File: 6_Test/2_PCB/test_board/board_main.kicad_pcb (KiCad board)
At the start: 4 copper layers, 93 parts, among them J1 PWR_Supply_Pins, J10 Chip_AVSS_GND_Jumpers, J11 Buffer_PWR_Jumper, J12 Reset_PWR_Jumpers, J13 Reset_Signal_Jumpers, J2 Analog_Input_Pins, J3 Digital_Input_Pins, J4 Digital_Output_Pins, J5 Chip_VDD_Jumpers, J6 BNC_Odd, J7 BNC_Even, J8 BNC_Jumpers, J9 Analog_Input_Jumpers, U1 TPS74501PDRVR, U2 ADA4807-1AKSZ-R7, U3 ADA4807-1AKSZ-R7, U4 TPS74501PDRVR, U5 SN74HC74DR, U6 CD4001BM96, U7 SN74ALVCH162827DLR

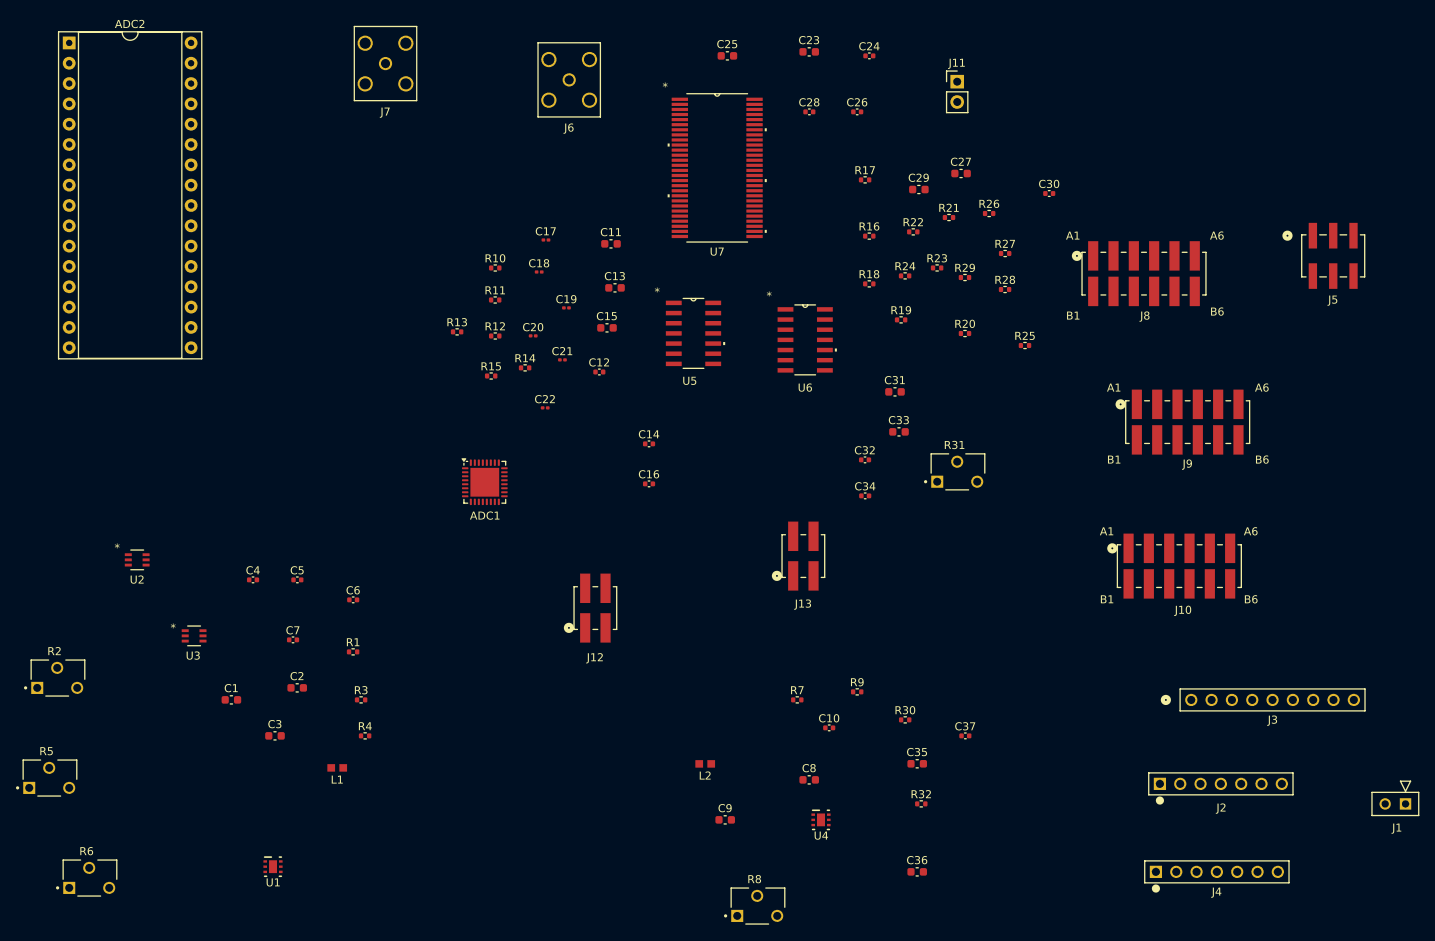
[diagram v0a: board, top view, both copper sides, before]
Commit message: Edit Layout 1_27
Rearranged the components in the layout and added majority of traces and ground layer. AVSS connections still need to be connected along with IOVDD
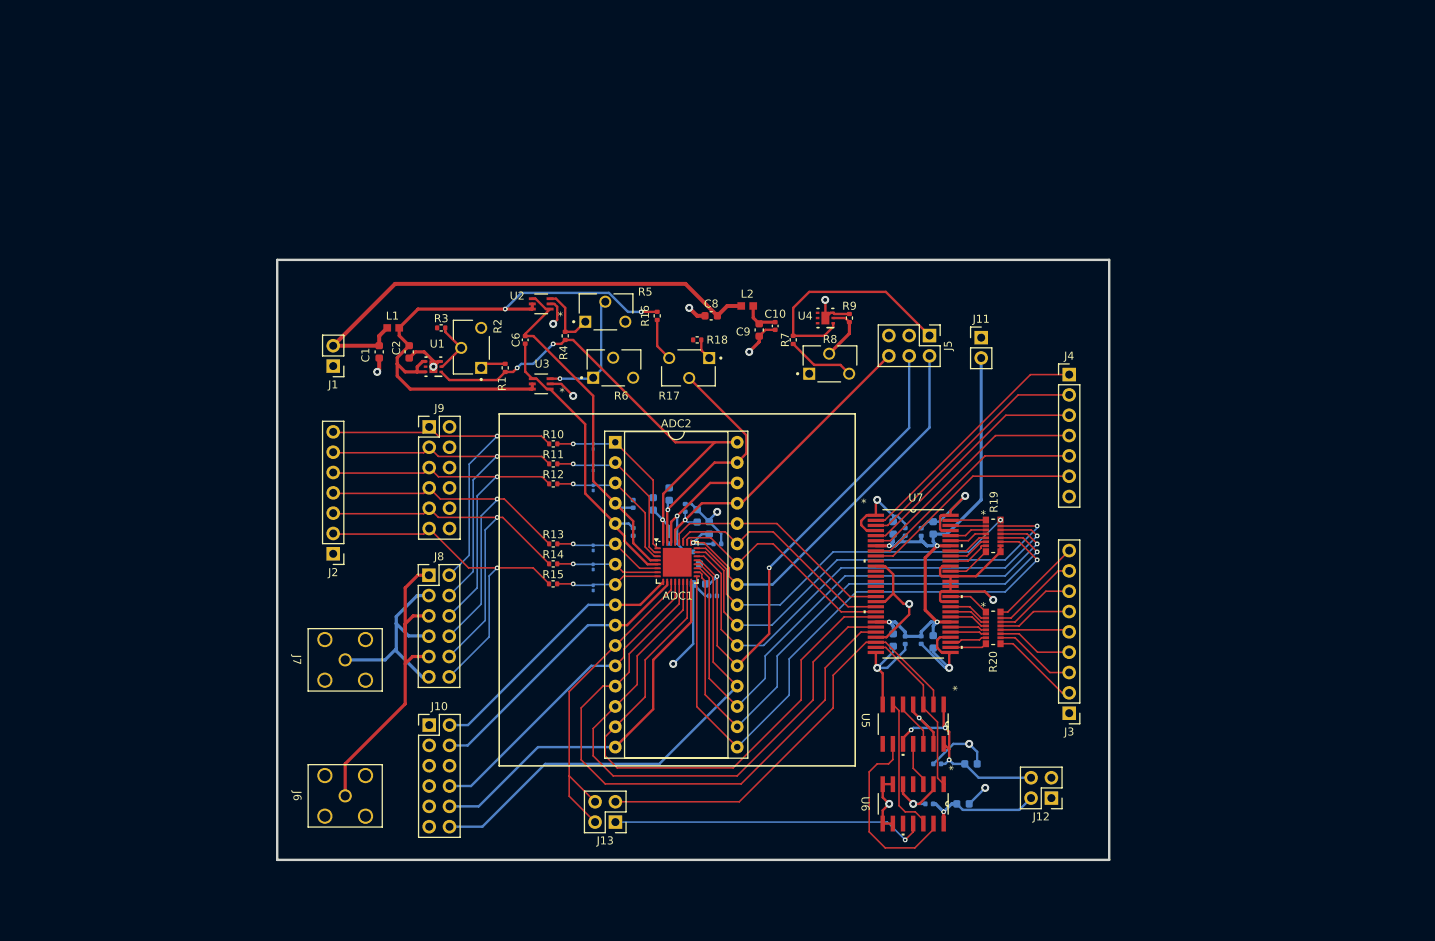
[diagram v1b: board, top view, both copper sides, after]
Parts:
- removed the R16 at (146.0, 61.5)
- removed the R17 at (145.5, 54.5)
- removed the R18 at (146.0, 67.5)
- removed R21, R22, R23, R24, R25, R26, R27, R28, R29: 22, Resistor_SMD:R_0402_1005Metric
- C11, C12, C13, C14, C15, C16, C17, C18, C19, C20, C21, C22, C23, C24, C25, C26, C27, C28, C29, C3, C30, C31, C32, C33, C34, C35, C36, C37, C4, C5, C7: moved to B.Cu
- J1: footprint ECE628_lib:1x2Header -> Connector_PinHeader_2.54mm:PinHeader_1x02_P2.54mm_Vertical
- J10, J8, J9: footprint ECE628_lib:2x6Header -> Connector_PinHeader_2.54mm:PinHeader_2x06_P2.54mm_Vertical
- J12, J13: footprint ECE628_lib:2x2Header -> Connector_PinHeader_2.54mm:PinHeader_2x02_P2.54mm_Vertical
- J2, J4: footprint ECE628_lib:1x7Header -> Connector_PinHeader_2.54mm:PinHeader_1x07_P2.54mm_Vertical
- J3: footprint ECE628_lib:1x9Header -> Connector_PinHeader_2.54mm:PinHeader_1x09_P2.54mm_Vertical
- J5: footprint ECE628_lib:2x3Header -> Connector_PinHeader_2.54mm:PinHeader_2x03_P2.54mm_Vertical
- R19, R20: value 22 -> EXB-2HV220JV; footprint Resistor_SMD:R_0402_1005Metric -> 22res_arrayFootprints:RES_EXB2HV
- moved J1 144.8 mm to (79.0, 77.8), turned to 180 degrees
- moved J2 107.3 mm to (79.0, 101.2), turned to 180 degrees
- moved J8 97.0 mm to (91.0, 103.9)
- moved J10 95.9 mm to (91.0, 122.7)
- moved J9 94.8 mm to (91.0, 85.4)
- moved J6 93.8 mm to (80.5, 131.5), turned to -90 degrees
- moved R6 91.4 mm to (114.0, 78.0)
- moved R5 90.7 mm to (113.0, 71.0)
- moved ADC2 84.6 mm to (114.3, 87.3)
- moved J7 74.7 mm to (80.5, 114.5), turned to -90 degrees
- moved R8 68.4 mm to (141.0, 77.5)
- moved C28 67.5 mm to (152.5, 112.0), turned to -90 degrees
- moved R2 66.2 mm to (96.3, 75.5), turned to 90 degrees
- moved U1 65.6 mm to (91.5, 77.8), turned to 180 degrees
- moved R18 64.4 mm to (124.5, 74.5), turned to 180 degrees
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- renumbered R30 to R16, R31 to R17, R32 to R18
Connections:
- J3 pad 2: /Buffer/RES_IND -> /Buffer/CLK_IND
- J3 pad 3: /Buffer/CLK_IND -> /Buffer/RES_IND
- J3 pad 4: /Buffer/CLK_IN6 -> /Buffer/CLK_IN4
- J3 pad 6: /Buffer/CLK_IN4 -> /Buffer/CLK_IN6
- J3 pad 7: /Buffer/CLK_IN3 -> /Buffer/CLK_IN1
- J3 pad 9: /Buffer/CLK_IN1 -> /Buffer/CLK_IN3
- R19 pad 1: /ADC/OUT4 -> Net-(U7-1A1)
- R19 pad 2: Net-(U7-2A7) -> Net-(U7-1A2)
- R20 pad 1: /ADC/OUT5 -> Net-(U7-2A3)
- R20 pad 2: Net-(U7-2A6) -> Net-(U7-2A4)
- U7 pad 10: /Buffer/CLKX -> unconnected-(U7-1Y7-Pad10)
- U7 pad 12: /Buffer/RESX -> unconnected-(U7-1Y8-Pad12)
- U7 pad 13: /ADC/CK6 -> unconnected-(U7-1Y9-Pad13)
- U7 pad 14: /ADC/CK5 -> unconnected-(U7-1Y10-Pad14)
- U7 pad 15: /ADC/CK4 -> unconnected-(U7-2Y1-Pad15)
- U7 pad 16: /ADC/CK3 -> unconnected-(U7-2Y2-Pad16)
- U7 pad 17: /ADC/CK2 -> /ADC/CK3
- U7 pad 19: /ADC/CK1 -> /ADC/CK2
- U7 pad 2: unconnected-(U7-1Y1-Pad2) -> /Buffer/DO1
- U7 pad 20: /Buffer/DO6 -> /ADC/CK1
- U7 pad 21: /Buffer/DO5 -> /ADC/CK6
- U7 pad 23: /Buffer/DO4 -> /ADC/CK5
- U7 pad 24: /Buffer/DO3 -> /ADC/CK4
- U7 pad 26: /Buffer/DO2 -> /Buffer/RESX
- U7 pad 27: /Buffer/DO1 -> /Buffer/CLKX
- U7 pad 3: unconnected-(U7-1Y2-Pad3) -> /Buffer/DO2
- U7 pad 41: Net-(U7-2A2) -> GND
- U7 pad 42: Net-(U7-2A1) -> GND
- U7 pad 43: Net-(U7-1A10) -> GND
- U7 pad 44: Net-(U7-1A9) -> GND
- U7 pad 48: GND -> Net-(U7-1A6)
- U7 pad 49: GND -> Net-(U7-1A5)
- U7 pad 5: unconnected-(U7-1Y3-Pad5) -> /Buffer/DO3
- U7 pad 51: GND -> Net-(U7-1A4)
- U7 pad 52: GND -> Net-(U7-1A3)
- U7 pad 54: GND -> Net-(U7-1A2)
- U7 pad 55: GND -> Net-(U7-1A1)
- U7 pad 6: unconnected-(U7-1Y4-Pad6) -> /Buffer/DO4
- U7 pad 8: unconnected-(U7-1Y5-Pad8) -> /Buffer/DO5
- U7 pad 9: unconnected-(U7-1Y6-Pad9) -> /Buffer/DO6
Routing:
- net GND: track 0.00 -> 175.8 mm, vias 0 -> 19
- net /ADC/OUT6: track 0.00 -> 78.8 mm, vias 0 -> 1
- net /ADC/CK4: track 0.00 -> 77.0 mm
- net /ADC/OUT5: track 0.00 -> 75.8 mm, vias 0 -> 1
- net /ADC/CK5: track 0.00 -> 73.7 mm
- net /ADC/OUT4: track 0.00 -> 72.2 mm, vias 0 -> 1
- net /ADC/CK6: track 0.00 -> 71.2 mm
- net /AnalogSupply/VA: track 0.00 -> 70.4 mm, vias 0 -> 2
- net /Buffer/VCC: track 0.00 -> 67.8 mm, vias 0 -> 4
- net Net-(ADC1-IOVDD-Pad21): track 0.00 -> 67.4 mm, vias 0 -> 2
- net /AnalogSupply/VSUP: track 0.00 -> 64.8 mm
- net /ADC/AVDD: track 0.00 -> 64.1 mm, vias 0 -> 3
- net /ADC/OUT3: track 0.00 -> 61.8 mm, vias 0 -> 1
- net Net-(ADC1-IOVSS-Pad20): track 0.00 -> 60.8 mm
- net /ADC/OUT2: track 0.00 -> 59.2 mm, vias 0 -> 1
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- added copper zone on In1.Cu, net GND
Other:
- board outline added: 104 x 75 mm

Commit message: Finished board layout
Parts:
- removed C34, C37: 100n, Capacitor_SMD:C_0402_1005Metric
- removed C35, C36: 4.7u, Capacitor_SMD:C_0603_1608Metric
- added R21: EXB-2HV220JV, 22res_arrayFootprints:RES_EXB2HV, F.Cu at (157.6, 94.5)
- added R22: EXB-2HV220JV, 22res_arrayFootprints:RES_EXB2HV, F.Cu at (157.5, 109.4)
- added U8: SN74LVC245APWR, SN74LVC245APWRFootprints:PW20, F.Cu at (150.0, 108.9)
- U7: value SN74ALVCH162827DLR -> SN74LVC245APWR; footprint 74ALVCHFootprints:DL56 -> SN74LVC245APWRFootprints:PW20
- moved C31 50.8 mm to (121.0, 93.5), turned to 90 degrees
- moved C33 45.3 mm to (124.0, 102.3), turned to -90 degrees
- moved C32 40.6 mm to (122.5, 102.5), turned to -90 degrees
- moved C29 22.4 mm to (158.0, 132.5), turned to 180 degrees
- moved C30 20.7 mm to (153.5, 132.5), turned to 0 degrees
- moved R19 18.7 mm to (143.5, 93.9)
- moved R20 18.5 mm to (143.1, 109.1)
- moved C27 16.1 mm to (159.0, 127.5), turned to 0 degrees
- moved C28 15.6 mm to (154.5, 127.5), turned to 180 degrees
- moved C24 11.6 mm to (151.0, 86.9), turned to 180 degrees
- moved U7 11.1 mm to (150.3, 94.0)
- moved C23 9.44 mm to (151.5, 88.9), turned to 180 degrees
- moved C25 6.43 mm to (150.5, 103.4), turned to 180 degrees
- moved C26 3.92 mm to (150.5, 101.9), turned to 180 degrees
- moved J4 3.64 mm to (167.5, 79.8)
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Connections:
- C27 pad 1: /Buffer/VCC -> Net-(U5-*1CLR)
- C28 pad 1: /Buffer/VCC -> Net-(U5-*1CLR)
- C29 pad 1: /Buffer/VCC -> GND
- C29 pad 2: GND -> Net-(U6-VDD)
- C30 pad 1: /Buffer/VCC -> GND
- C30 pad 2: GND -> Net-(U6-VDD)
- C31 pad 1: Net-(U5-*1CLR) -> /ADC/VREF
- C31 pad 2: GND -> /ADC/AVSS
- C32 pad 1: Net-(U5-*1CLR) -> /ADC/VLDO
- C32 pad 2: GND -> /ADC/AVSS
- C33 pad 1: GND -> /ADC/VLDO
- C33 pad 2: Net-(U6-VDD) -> /ADC/AVSS
- R19 pad 1: Net-(U7-1A1) -> /ADC/OUT1
- R19 pad 10: GND -> Net-(U7-A7)
- R19 pad 11: /ADC/OUT6 -> Net-(U7-A6)
- R19 pad 12: /ADC/OUT5 -> Net-(U7-A5)
- R19 pad 13: /ADC/OUT4 -> Net-(U7-A4)
- R19 pad 14: /ADC/OUT3 -> Net-(U7-A3)
- R19 pad 15: /ADC/OUT2 -> Net-(U7-A2)
- R19 pad 16: /ADC/OUT1 -> Net-(U7-A1)
- R19 pad 2: Net-(U7-1A2) -> /ADC/OUT2
- R19 pad 3: Net-(U7-1A3) -> /ADC/OUT3
- R19 pad 4: Net-(U7-1A4) -> /ADC/OUT4
- R19 pad 5: Net-(U7-1A5) -> /ADC/OUT5
- R19 pad 6: Net-(U7-1A6) -> /ADC/OUT6
- R19 pad 7: Net-(U7-1A7) -> GND
- R19 pad 8: Net-(U7-1A8) -> GND
- R19 pad 9: GND -> Net-(U7-A8)
- R20 pad 1: Net-(U7-2A3) -> /ADC/CK3
- R20 pad 10: /Buffer/RES_IND -> Net-(U8-A7)
- R20 pad 11: /Buffer/CLK_IN4 -> Net-(U8-A6)
- R20 pad 12: /Buffer/CLK_IN5 -> Net-(U8-A5)
- R20 pad 13: /Buffer/CLK_IN6 -> Net-(U8-A4)
- R20 pad 14: /Buffer/CLK_IN1 -> Net-(U8-A3)
- R20 pad 15: /Buffer/CLK_IN2 -> Net-(U8-A2)
- R20 pad 16: /Buffer/CLK_IN3 -> Net-(U8-A1)
- R20 pad 2: Net-(U7-2A4) -> /ADC/CK2
- R20 pad 3: Net-(U7-2A5) -> /ADC/CK1
- R20 pad 4: Net-(U7-2A6) -> /ADC/CK6
- R20 pad 5: Net-(U7-2A7) -> /ADC/CK5
- R20 pad 6: Net-(U7-2A8) -> /ADC/CK4
- R20 pad 7: Net-(U7-2A9) -> /Buffer/RESX
- R20 pad 8: Net-(U7-2A10) -> /Buffer/CLKX
- R20 pad 9: /Buffer/CLK_IND -> Net-(U8-A8)
- U7 pad 1: GND -> /Buffer/VCC
- U7 pad 10: unconnected-(U7-1Y7-Pad10) -> GND
- U7 pad 11: GND -> Net-(U7-B8)
- U7 pad 12: unconnected-(U7-1Y8-Pad12) -> Net-(U7-B7)
- U7 pad 13: unconnected-(U7-1Y9-Pad13) -> Net-(U7-B6)
- U7 pad 14: unconnected-(U7-1Y10-Pad14) -> Net-(U7-B5)
- U7 pad 15: unconnected-(U7-2Y1-Pad15) -> Net-(U7-B4)
- U7 pad 16: unconnected-(U7-2Y2-Pad16) -> Net-(U7-B3)
- U7 pad 17: /ADC/CK3 -> Net-(U7-B2)
- U7 pad 18: GND -> Net-(U7-B1)
- U7 pad 19: /ADC/CK2 -> GND
- U7 pad 2: /Buffer/DO1 -> Net-(U7-A1)
- U7 pad 20: /ADC/CK1 -> /Buffer/VCC
- U7 pad 3: /Buffer/DO2 -> Net-(U7-A2)
- U7 pad 4: GND -> Net-(U7-A3)
- U7 pad 5: /Buffer/DO3 -> Net-(U7-A4)
- U7 pad 6: /Buffer/DO4 -> Net-(U7-A5)
- U7 pad 7: /Buffer/VCC -> Net-(U7-A6)
- U7 pad 8: /Buffer/DO5 -> Net-(U7-A7)
- U7 pad 9: /Buffer/DO6 -> Net-(U7-A8)
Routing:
- net /ADC/IOVDD: track 4.62 -> 104.4 mm, vias 0 -> 2
- net GND: track 175.8 -> 130.8 mm, vias 19 -> 15
- net /ADC/AVSS: track 0.00 -> 35.4 mm, vias 0 -> 9
- net /Buffer/VCC: track 67.8 -> 43.0 mm, vias 4 -> 2
- net /ADC/OUT2: track 59.2 -> 35.6 mm
- net /ADC/OUT3: track 61.8 -> 39.5 mm
- net /ADC/OUT4: track 72.2 -> 52.4 mm
- net /ADC/OUT5: track 75.8 -> 56.3 mm
- net /ADC/OUT6: track 78.8 -> 60.0 mm
- net /Buffer/DO6: track 28.3 -> 10.1 mm
- net /Buffer/DO5: track 29.1 -> 11.0 mm
- net /Buffer/DO4: track 29.6 -> 11.8 mm
- net /Buffer/DO3: track 30.4 -> 12.9 mm
- net /Buffer/DO2: track 30.9 -> 15.4 mm
- net /Buffer/DO1: track 31.7 -> 16.3 mm
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- added copper zone on In2.Cu, net /ADC/AVSS
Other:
- board size 104 x 75 mm -> 100.5 x 75 mm

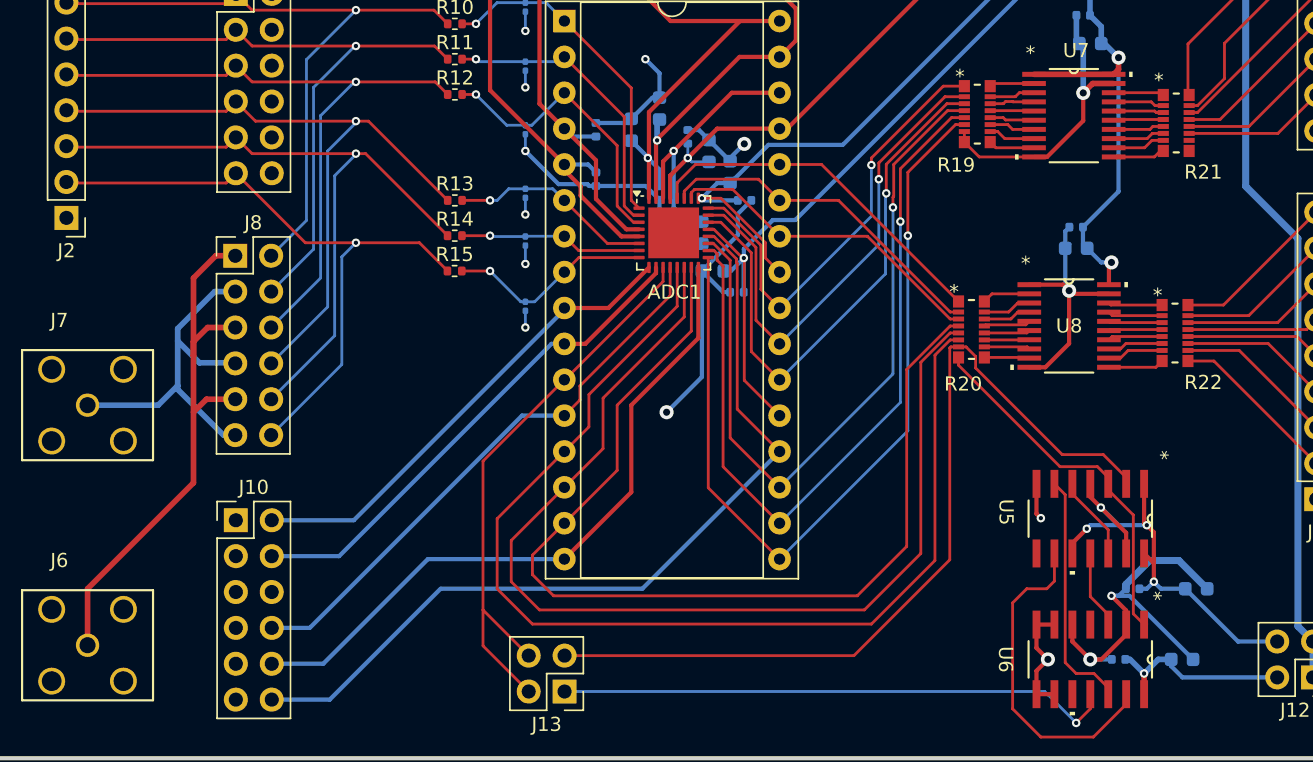
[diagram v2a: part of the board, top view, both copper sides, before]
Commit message: Refining board layout & 3D model
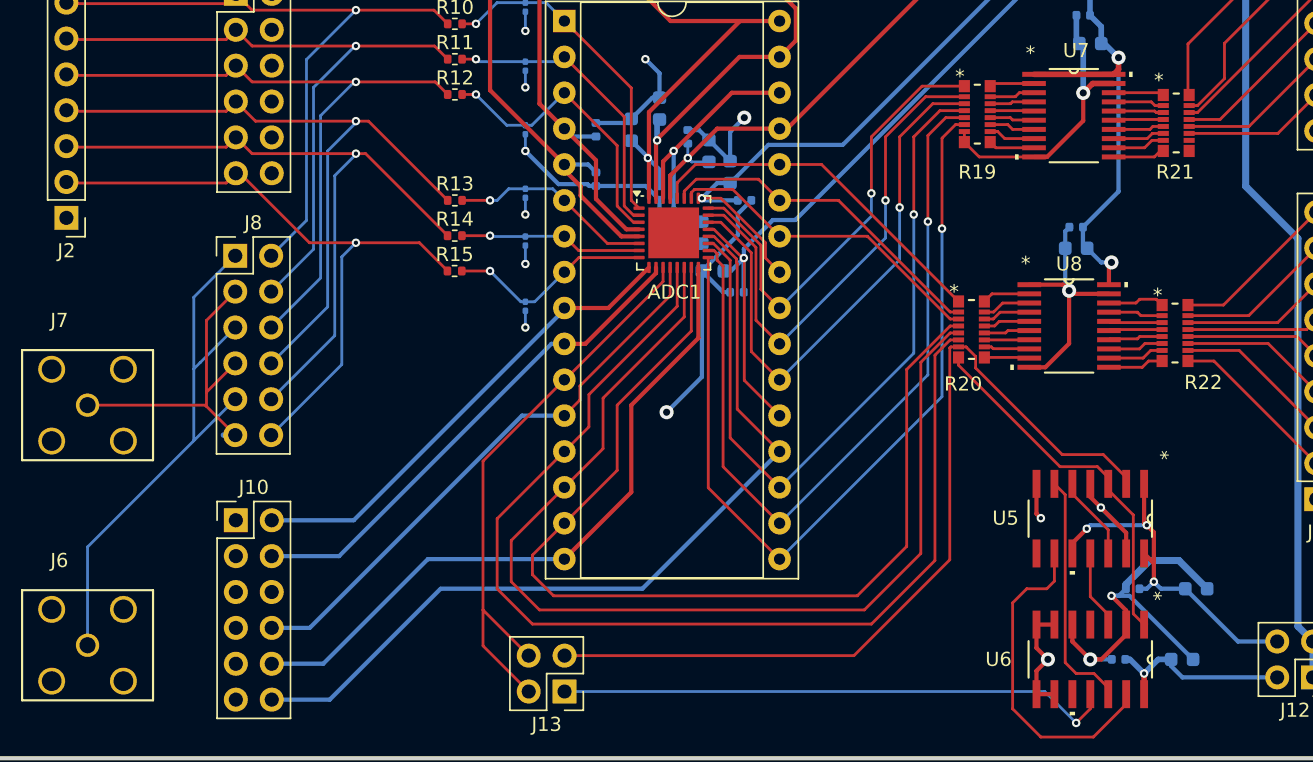
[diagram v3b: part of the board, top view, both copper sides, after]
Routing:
- net Net-(J7-Signal): track 26.6 -> 24.0 mm
- net GND: track 130.8 -> 132.7 mm
- net /ADC/OUT1: track 31.8 -> 32.7 mm
- net /ADC/OUT2: track 35.6 -> 36.4 mm
- net /ADC/OUT3: track 39.5 -> 40.0 mm
